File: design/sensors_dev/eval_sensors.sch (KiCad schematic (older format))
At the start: 34 parts, among them J4 Conn_01x12, U2 BMC150, U3 LSM6DS3HTR, U4 FXAS21002, U5 MS5607-02BA03, U6 LIS3DHTR

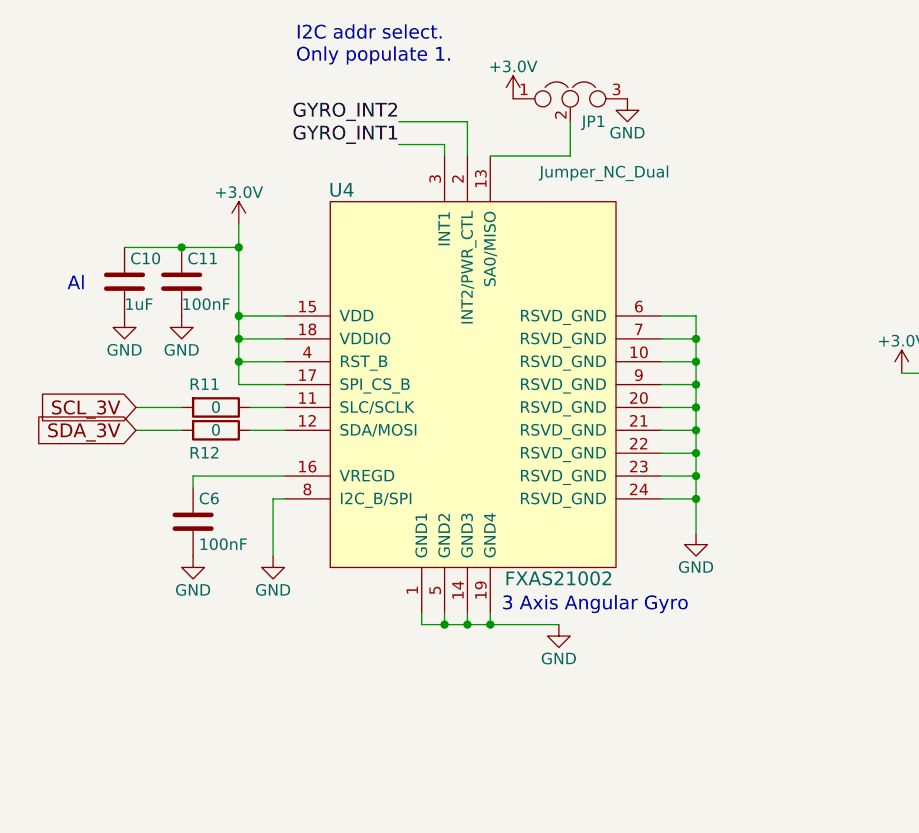
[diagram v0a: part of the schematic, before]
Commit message: Start PCB and swap out gyro
Old gyro (fxas) was 24 LGA and required a clearance between 3 and 4 mil,
which increases costs and cuts down fab house options. Swapped out the
gyro for another one with slightly higher drift but in a more convenient
package (LGA14).
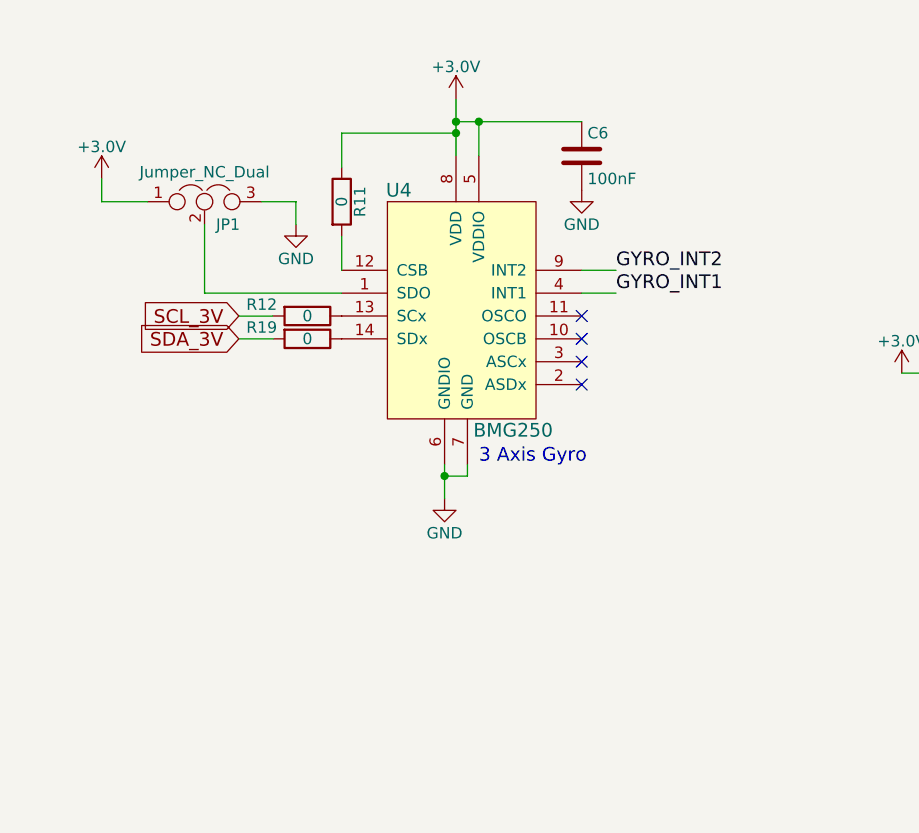
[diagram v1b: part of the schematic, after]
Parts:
- removed C10: 1uF, Capacitors_ThroughHole:CP_Radial_Tantal_D5.0mm_P2.50mm, symbol C
- removed C11: 100nF, Capacitors_SMD:C_0805_HandSoldering, symbol C
- removed U4: FXAS21002, Package_DFN_QFN:QFN-24_4x4mm_P0.5mm, symbol FXAS21002
- added R19: 0, Capacitors_SMD:C_0805_HandSoldering, symbol R
- added U4: BMG250, Package_LGA:Bosch_LGA-14_3x2.5mm_P0.5mm, symbol BMG250
- R11, R12: footprint Resistors_SMD:R_0805_HandSoldering -> Capacitors_SMD:C_0805_HandSoldering
- U3: footprint Package_LGA:Bosch_LGA-14_3x2.5mm_P0.5mm -> LSM6DS3:PQFN50P300X250X86-14N
- U5: footprint (none) -> MS560702BA03-50:SON125P300X500X100-8N
- U6: footprint (none) -> LIS3DHTR:LGA16R50P5X3_300X300X100N
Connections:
- net +3.0V: now also C6.1, R11.1, U4.5 (VDDIO), U4.8 (VDD)
- net GND: now also U4.6 (GNDIO), U4.7 (GND)
- net GYRO_INT1: now also U4.4 (INT1)
- net GYRO_INT2: now also U4.9 (INT2)
- net SCL_3V: now also R12.2; no longer R11.2
- net SDA_3V: now also R19.2; no longer R12.2
- net at R12.1: now also U4.13 (SCx)
- net at JP1.2: now also U4.1 (SDO)
- new net: R11.2, U4.12 (CSB)
- new net: R19.1, U4.14 (SDx)
- no-connect marks 7 -> 11
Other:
- note added: "3 Axis Gyro"
- note removed: "3 Axis Angular Gyro"
- note removed: "Al\n"

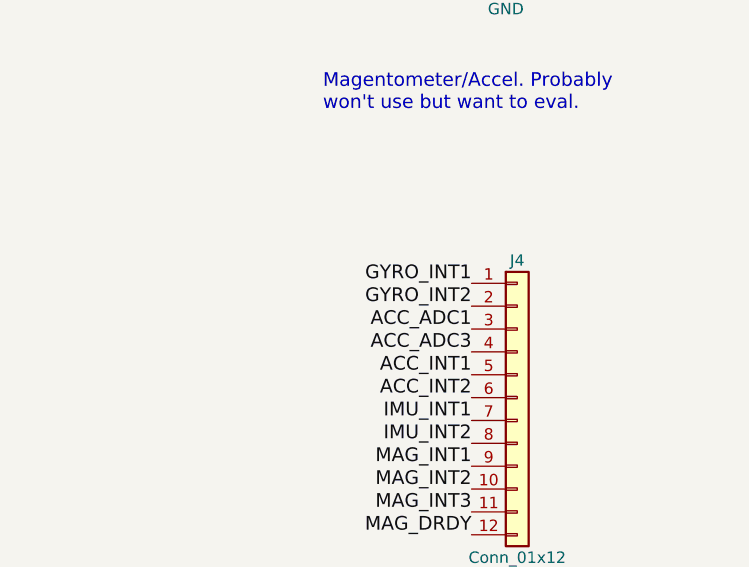
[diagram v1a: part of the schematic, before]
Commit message: First pass board routing.
Also, remove arduino from PCB since this is a dev board and there's no
point paying for extra unused board space.
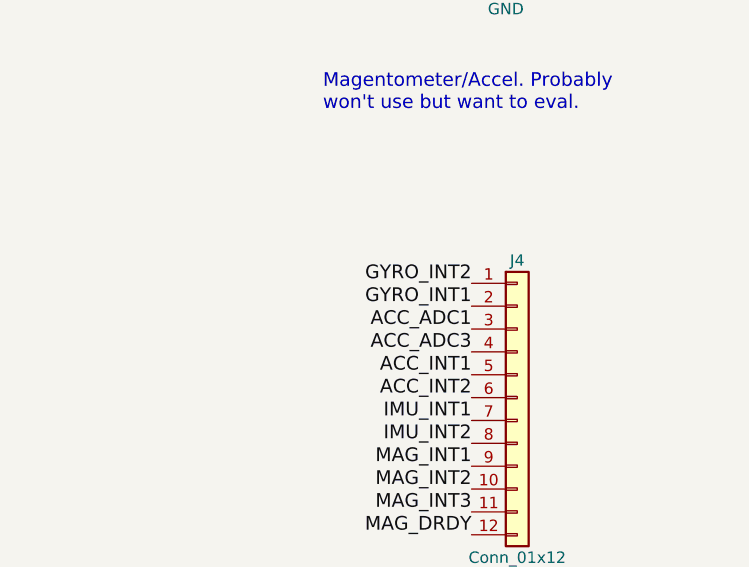
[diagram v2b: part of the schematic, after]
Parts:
- U2, U4: footprint Package_LGA:Bosch_LGA-14_3x2.5mm_P0.5mm -> footprints:Bosch_LGA-14
- U5: footprint MS560702BA03-50:SON125P300X500X100-8N -> footprints:MS560702BA03
- U6: footprint LIS3DHTR:LGA16R50P5X3_300X300X100N -> footprints:LGA16_LIS3DHTR
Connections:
- net GYRO_INT1: now also J4.2 (Pin_2); no longer J4.1 (Pin_1)
- net GYRO_INT2: now also J4.1 (Pin_1); no longer J4.2 (Pin_2)
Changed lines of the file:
@@
 F 0 "U2" H 9400 3000 60  0000 C CNN
 F 1 "BMC150" H 10050 2050 60  0000 C CNN
-F 2 "Package_LGA:Bosch_LGA-14_3x2.5mm_P0.5mm" H 9700 2550 60  0001 C CNN
+F 2 "footprints:Bosch_LGA-14" H 9700 2550 60  0001 C CNN
 F 3 "" H 9700 2550 60  0001 C CNN
 	1    9700 2550
@@
 F 0 "U6" H 2650 6650 60  0000 C CNN
 F 1 "LIS3DHTR" H 3350 5700 60  0000 C CNN
-F 2 "LIS3DHTR:LGA16R50P5X3_300X300X100N" H 2950 6100 60  0001 C CNN
+F 2 "footprints:LGA16_LIS3DHTR" H 2950 6100 60  0001 C CNN
 F 3 "" H 2950 6100 60  0001 C CNN
 	1    2950 6100
@@
 F 0 "U5" H 5850 6000 60  0000 C CNN
 F 1 "MS5607-02BA03" H 6100 5450 60  0000 C CNN
-F 2 "MS560702BA03-50:SON125P300X500X100-8N" H 6100 5450 60  0001 C CNN
+F 2 "footprints:MS560702BA03" H 6100 5450 60  0001 C CNN
 F 3 "" H 6100 5450 60  0001 C CNN
 	1    6050 5450
@@
 $EndComp
 $Comp
-L GND #PWR016
+L GND #PWR015
 U 1 1 5AAC81D4
 P 6450 3250
-F 0 "#PWR016" H 6450 3000 50  0001 C CNN
+F 0 "#PWR015" H 6450 3000 50  0001 C CNN
 F 1 "GND" H 6450 3100 50  0000 C CNN
 F 2 "" H 6450 3250 50  0001 C CNN
@@
 NoConn ~ 6650 1950
 $Comp
-L +3.0V #PWR017
+L +3.0V #PWR016
 U 1 1 5AAC81DC
 P 6550 1650
-F 0 "#PWR017" H 6550 1500 50  0001 C CNN
+F 0 "#PWR016" H 6550 1500 50  0001 C CNN
 F 1 "+3.0V" H 6550 1790 50  0000 C CNN
 F 2 "" H 6550 1650 50  0001 C CNN
@@
 $EndComp
 $Comp
-L GND #PWR018
+L GND #PWR017
 U 1 1 5AAC81E9
 P 6950 1750
-F 0 "#PWR018" H 6950 1500 50  0001 C CNN
+F 0 "#PWR017" H 6950 1500 50  0001 C CNN
 F 1 "GND" H 6950 1600 50  0000 C CNN
 F 2 "" H 6950 1750 50  0001 C CNN
@@
 $EndComp
 $Comp
-L GND #PWR019
+L GND #PWR018
 U 1 1 5AAC81EF
 P 7300 2900
-F 0 "#PWR019" H 7300 2650 50  0001 C CNN
+F 0 "#PWR018" H 7300 2650 50  0001 C CNN
 F 1 "GND" H 7300 2750 50  0000 C CNN
 F 2 "" H 7300 2900 50  0001 C CNN
@@
 $EndComp
 $Comp
-L +3.0V #PWR020
+L +3.0V #PWR019
 U 1 1 5AAC820F
 P 4650 2800
-F 0 "#PWR020" H 4650 2650 50  0001 C CNN
+F 0 "#PWR019" H 4650 2650 50  0001 C CNN
 F 1 "+3.0V" H 4650 2940 50  0000 C CNN
 F 2 "" H 4650 2800 50  0001 C CNN
@@
 $EndComp
 $Comp
-L +3.0V #PWR021
+L +3.0V #PWR020
 U 1 1 5AAC8232
 P 5200 4950
-F 0 "#PWR021" H 5200 4800 50  0001 C CNN
+F 0 "#PWR020" H 5200 4800 50  0001 C CNN
 F 1 "+3.0V" H 5200 5090 50  0000 C CNN
 F 2 "" H 5200 4950 50  0001 C CNN
@@
 $EndComp
 $Comp
-L GND #PWR022
+L GND #PWR021
 U 1 1 5AAC8238
 P 5200 5500
-F 0 "#PWR022" H 5200 5250 50  0001 C CNN
+F 0 "#PWR021" H 5200 5250 50  0001 C CNN
 F 1 "GND" H 5200 5350 50  0000 C CNN
 F 2 "" H 5200 5500 50  0001 C CNN
@@
 Barometer/Temperature
 $Comp
-L +3.0V #PWR023
+L +3.0V #PWR022
 U 1 1 5AAC8269
 P 8550 2450
-F 0 "#PWR023" H 8550 2300 50  0001 C CNN
+F 0 "#PWR022" H 8550 2300 50  0001 C CNN
 F 1 "+3.0V" H 8550 2590 50  0000 C CNN
 F 2 "" H 8550 2450 50  0001 C CNN
@@
 $EndComp
 $Comp
-L GND #PWR024
+L GND #PWR023
 U 1 1 5AAC8299
 P 9900 3250
-F 0 "#PWR024" H 9900 3000 50  0001 C CNN
+F 0 "#PWR023" H 9900 3000 50  0001 C CNN
 F 1 "GND" H 9900 3100 50  0000 C CNN
 F 2 "" H 9900 3250 50  0001 C CNN
@@
 $EndComp
 $Comp
-L +3.0V #PWR025
+L +3.0V #PWR024
 U 1 1 5AAC829F
 P 9600 1600
-F 0 "#PWR025" H 9600 1450 50  0001 C CNN
+F 0 "#PWR024" H 9600 1450 50  0001 C CNN
 F 1 "+3.0V" H 9600 1740 50  0000 C CNN
 F 2 "" H 9600 1600 50  0001 C CNN
@@
 $EndComp
 $Comp
-L GND #PWR026
+L GND #PWR025
 U 1 1 5AAC82B8
 P 10200 2000
-F 0 "#PWR026" H 10200 1750 50  0001 C CNN
+F 0 "#PWR025" H 10200 1750 50  0001 C CNN
 F 1 "GND" H 10200 1850 50  0000 C CNN
 F 2 "" H 10200 2000 50  0001 C CNN
@@
 $EndComp
 $Comp
-L GND #PWR027
+L GND #PWR026
 U 1 1 5AAC82BE
 P 10450 2000
-F 0 "#PWR027" H 10450 1750 50  0001 C CNN
+F 0 "#PWR026" H 10450 1750 50  0001 C CNN
 F 1 "GND" H 10450 1850 50  0000 C CNN
 F 2 "" H 10450 2000 50  0001 C CNN
@@
 $EndComp
 $Comp
-L GND #PWR028
+L GND #PWR027
 U 1 1 5AAC82D9
 P 5600 5300
-F 0 "#PWR028" H 5600 5050 50  0001 C CNN
+F 0 "#PWR027" H 5600 5050 50  0001 C CNN
 F 1 "GND" H 5600 5150 50  0000 C CNN
 F 2 "" H 5600 5300 50  0001 C CNN
@@
 $EndComp
 $Comp
-L +3.0V #PWR029
+L +3.0V #PWR028
 U 1 1 5AAC8310
 P 1350 6150
-F 0 "#PWR029" H 1350 6000 50  0001 C CNN
+F 0 "#PWR028" H 1350 6000 50  0001 C CNN
 F 1 "+3.0V" H 1350 6290 50  0000 C CNN
 F 2 "" H 1350 6150 50  0001 C CNN
@@
 NoConn ~ 3100 6600
 $Comp
-L GND #PWR030
+L GND #PWR029
 U 1 1 5AAC8318
 P 2800 6700
-F 0 "#PWR030" H 2800 6450 50  0001 C CNN
+F 0 "#PWR029" H 2800 6450 50  0001 C CNN
 F 1 "GND" H 2800 6550 50  0000 C CNN
 F 2 "" H 2800 6700 50  0001 C CNN
@@
 NoConn ~ 3100 5400
 $Comp
-L GND #PWR031
+L GND #PWR030
 U 1 1 5AAC8323
 P 3500 6200
-F 0 "#PWR031" H 3500 5950 50  0001 C CNN
+F 0 "#PWR030" H 3500 5950 50  0001 C CNN
 F 1 "GND" H 3500 6050 50  0000 C CNN
 F 2 "" H 3500 6200 50  0001 C CNN
@@
 $EndComp
 $Comp
-L +3.0V #PWR032
+L +3.0V #PWR031
 U 1 1 5AAC8329
 P 2800 5050
-F 0 "#PWR032" H 2800 4900 50  0001 C CNN
+F 0 "#PWR031" H 2800 4900 50  0001 C CNN
 F 1 "+3.0V" H 2800 5190 50  0000 C CNN
 F 2 "" H 2800 5050 50  0001 C CNN
@@
 $EndComp
 $Comp
-L GND #PWR033
+L GND #PWR032
 U 1 1 5AAC8387
 P 3550 5400
-F 0 "#PWR033" H 3550 5150 50  0001 C CNN
+F 0 "#PWR032" H 3550 5150 50  0001 C CNN
 F 1 "GND" H 3550 5250 50  0000 C CNN
 F 2 "" H 3550 5400 50  0001 C CNN
@@
 $EndComp
 $Comp
-L GND #PWR034
+L GND #PWR033
 U 1 1 5AAC838D
 P 3800 5400
-F 0 "#PWR034" H 3800 5150 50  0001 C CNN
+F 0 "#PWR033" H 3800 5150 50  0001 C CNN
 F 1 "GND" H 3800 5250 50  0000 C CNN
 F 2 "" H 3800 5400 50  0001 C CNN
@@
 	1    0    0    -1
 $EndComp
+Text Label 9750 4600 2    60   ~ 0
+GYRO_INT2
 Text Label 9750 4700 2    60   ~ 0
-GYRO_INT2
-Text Label 9750 4600 2    60   ~ 0
 GYRO_INT1
 Text Label 9750 4800 2    60   ~ 0
@@
 $EndComp
 $Comp
-L +3.0V #PWR035
+L +3.0V #PWR034
 U 1 1 5AACCD77
 P 5150 2200
-F 0 "#PWR035" H 5150 2050 50  0001 C CNN
+F 0 "#PWR034" H 5150 2050 50  0001 C CNN
 F 1 "+3.0V" H 5150 2340 50  0000 C CNN
 F 2 "" H 5150 2200 50  0001 C CNN
@@
 $EndComp
 $Comp
-L GND #PWR036
+L GND #PWR035
 U 1 1 5AACCE90
 P 5850 2200
-F 0 "#PWR036" H 5850 1950 50  0001 C CNN
+F 0 "#PWR035" H 5850 1950 50  0001 C CNN
 F 1 "GND" H 5850 2050 50  0000 C CNN
 F 2 "" H 5850 2200 50  0001 C CNN
@@
 $EndComp
 $Comp
-L +3.0V #PWR037
+L +3.0V #PWR036
 U 1 1 5AACD859
 P 8450 1900
-F 0 "#PWR037" H 8450 1750 50  0001 C CNN
+F 0 "#PWR036" H 8450 1750 50  0001 C CNN
 F 1 "+3.0V" H 8450 2040 50  0000 C CNN
 F 2 "" H 8450 1900 50  0001 C CNN
@@
 $EndComp
 $Comp
-L GND #PWR038
+L GND #PWR037
 U 1 1 5AACD972
 P 9150 2050
-F 0 "#PWR038" H 9150 1800 50  0001 C CNN
+F 0 "#PWR037" H 9150 1800 50  0001 C CNN
 F 1 "GND" H 9150 1900 50  0000 C CNN
 F 2 "" H 9150 2050 50  0001 C CNN
@@
 $EndComp
 $Comp
-L +3.0V #PWR039
+L +3.0V #PWR038
 U 1 1 5AACED92
 P 6100 4450
-F 0 "#PWR039" H 6100 4300 50  0001 C CNN
+F 0 "#PWR038" H 6100 4300 50  0001 C CNN
 F 1 "+3.0V" H 6100 4590 50  0000 C CNN
 F 2 "" H 6100 4450 50  0001 C CNN
@@
 $EndComp
 $Comp
-L GND #PWR040
+L GND #PWR039
 U 1 1 5AACEEA7
 P 6950 4650
-F 0 "#PWR040" H 6950 4400 50  0001 C CNN
+F 0 "#PWR039" H 6950 4400 50  0001 C CNN
 F 1 "GND" H 6950 4500 50  0000 C CNN
 F 2 "" H 6950 4650 50  0001 C CNN
@@
 $EndComp
 $Comp
-L +3.0V #PWR041
+L +3.0V #PWR040
 U 1 1 5AACF902
 P 1600 5350
-F 0 "#PWR041" H 1600 5200 50  0001 C CNN
+F 0 "#PWR040" H 1600 5200 50  0001 C CNN
 F 1 "+3.0V" H 1600 5490 50  0000 C CNN
 F 2 "" H 1600 5350 50  0001 C CNN
@@
 $EndComp
 $Comp
-L GND #PWR042
+L GND #PWR041
 U 1 1 5AACFA16
 P 2400 5500
-F 0 "#PWR042" H 2400 5250 50  0001 C CNN
+F 0 "#PWR041" H 2400 5250 50  0001 C CNN
 F 1 "GND" H 2400 5350 50  0000 C CNN
 F 2 "" H 2400 5500 50  0001 C CNN
@@
 Al
 $Comp
-L GND #PWR043
+L GND #PWR042
 U 1 1 5AB14238
 P 2650 3350
-F 0 "#PWR043" H 2650 3100 50  0001 C CNN
+F 0 "#PWR042" H 2650 3100 50  0001 C CNN
 F 1 "GND" H 2650 3200 50  0000 C CNN
 F 2 "" H 2650 3350 50  0001 C CNN
@@
 NoConn ~ 3250 2850
 $Comp
-L +3.0V #PWR044
+L +3.0V #PWR043
 U 1 1 5AB15C93
 P 2700 1600
-F 0 "#PWR044" H 2700 1450 50  0001 C CNN
+F 0 "#PWR043" H 2700 1450 50  0001 C CNN
 F 1 "+3.0V" H 2700 1740 50  0000 C CNN
 F 2 "" H 2700 1600 50  0001 C CNN
@@
 $EndComp
 $Comp
-L GND #PWR045
+L GND #PWR044
 U 1 1 5AB162FC
 P 3250 2000
-F 0 "#PWR045" H 3250 1750 50  0001 C CNN
+F 0 "#PWR044" H 3250 1750 50  0001 C CNN
 F 1 "GND" H 3250 1850 50  0000 C CNN
 F 2 "" H 3250 2000 50  0001 C CNN
@@
 	1600 2450 2200 2450
 $Comp
-L +3.0V #PWR046
+L +3.0V #PWR045
 U 1 1 5AB17003
 P 1150 1950
-F 0 "#PWR046" H 1150 1800 50  0001 C CNN
+F 0 "#PWR045" H 1150 1800 50  0001 C CNN
 F 1 "+3.0V" H 1150 2090 50  0000 C CNN
 F 2 "" H 1150 1950 50  0001 C CNN
@@
 	1150 2050 1350 2050
 $Comp
-L GND #PWR047
+L GND #PWR046
 U 1 1 5AB170F5
 P 2000 2150
-F 0 "#PWR047" H 2000 1900 50  0001 C CNN
+F 0 "#PWR046" H 2000 1900 50  0001 C CNN
 F 1 "GND" H 2000 2000 50  0000 C CNN
 F 2 "" H 2000 2150 50  0001 C CNN
@@
 F 0 "U4" H 2450 3500 60  0000 C CNN
 F 1 "BMG250" H 2950 2450 60  0000 C CNN
-F 2 "Package_LGA:Bosch_LGA-14_3x2.5mm_P0.5mm" H 2650 2750 60  0001 C CNN
+F 2 "footprints:Bosch_LGA-14" H 2650 2750 60  0001 C CNN
 F 3 "" H 2650 2750 60  0001 C CNN
 	1    2750 2750
